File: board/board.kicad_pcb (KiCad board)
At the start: 2 copper layers, 41.1 x 15.7 mm, 14 parts, among them J1 Conn_01x05, P1 USB_C_Plug_USB2.0, U1 FT232RL

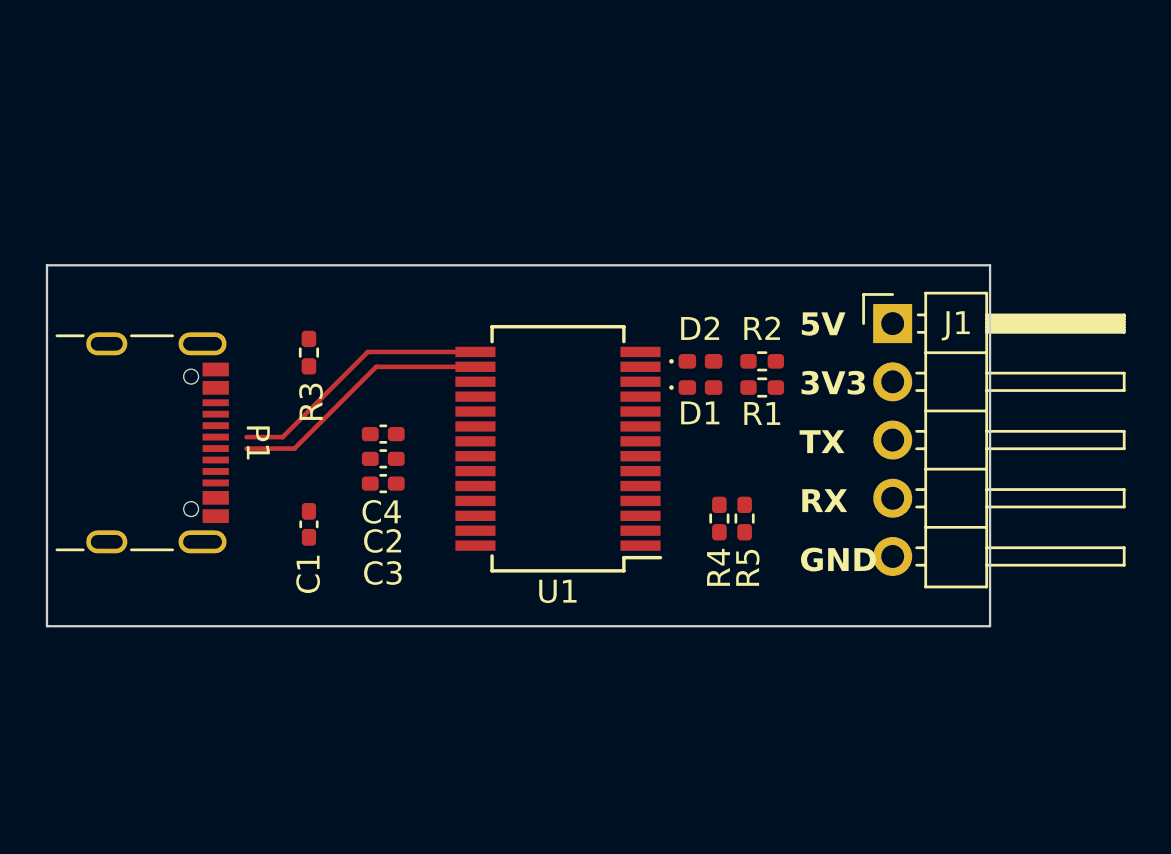
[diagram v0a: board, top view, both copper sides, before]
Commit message: feat(bsp/usb-ttl/debug): schematic
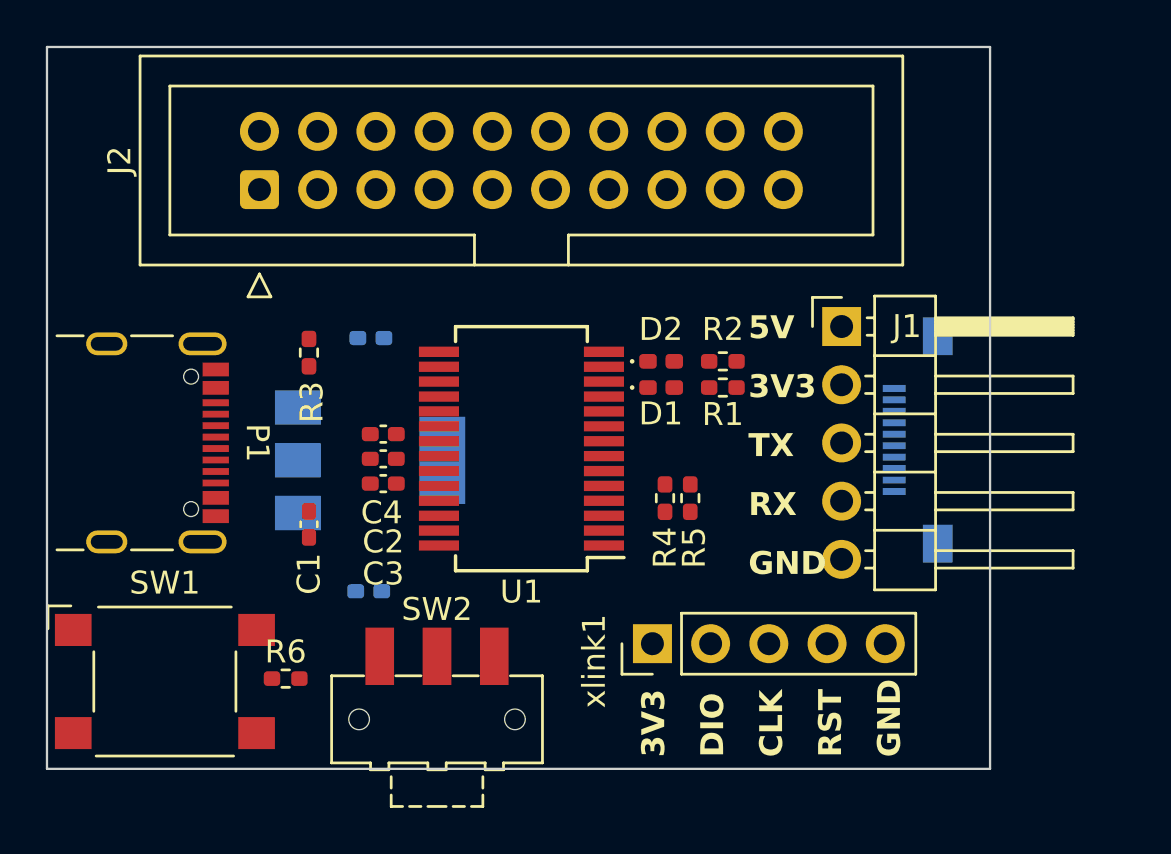
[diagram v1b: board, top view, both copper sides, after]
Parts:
- added C5: 10uF, Capacitor_SMD:C_0402_1005Metric_Pad0.74x0.62mm_HandSolder, B.Cu at (102.7, 90.6)
- added C6: 10uF, Capacitor_SMD:C_0402_1005Metric_Pad0.74x0.62mm_HandSolder, B.Cu at (102.6, 101.6)
- added J2: Conn_ARM_JTAG_SWD_20, Connector_IDC:IDC-Header_2x10_P2.54mm_Vertical, F.Cu at (97.8, 84.1)
- added J3: Conn_01x10, Connector_FFC-FPC:Molex_54548-1071_1x10-1MP_P0.5mm_Horizontal, B.Cu at (126.5, 95.0)
- added R6: 10K, Resistor_SMD:R_0402_1005Metric_Pad0.72x0.64mm_HandSolder, F.Cu at (98.9, 105.4)
- added SW1: RST, Button_Switch_SMD:SW_SPST_Omron_B3FS-100xP, F.Cu at (93.7, 105.5)
- added SW2: BOOT, Button_Switch_SMD:SW_SPDT_CK-JS102011SAQN, F.Cu at (105.5, 107.2)
- added U2: AMS1117-3.3, Package_TO_SOT_SMD:SOT-223-3_TabPin2, B.Cu at (102.6, 95.9)
- added xlink1: Conn_01x05, Connector_PinHeader_2.54mm:PinHeader_1x05_P2.54mm_Vertical, F.Cu at (114.9, 103.9)
- moved R4 2.53 mm to (115.5, 97.5)
- moved R5 2.53 mm to (116.6, 97.5)
- moved J1 2.23 mm to (123.2, 90.0)
- moved R1 1.72 mm to (118.0, 92.7)
- moved R2 1.72 mm to (118.0, 91.6)
- moved D1 1.72 mm to (115.3, 92.7)
- moved D2 1.72 mm to (115.3, 91.6)
- moved U1 1.59 mm to (109.2, 95.4)
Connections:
- C4 pad 1: +3.3V -> /3V3
- U1 pad 17: +3.3V -> /3V3
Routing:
- net /D+: track 11.5 -> 0.00 mm
- net /D-: track 11.5 -> 0.00 mm
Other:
- board size 41.1 x 15.7 mm -> 41.1 x 31.5 mm
- board text added: "CLK"
- board text added: "DIO"
- board text added: "RST"

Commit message: feat(bsp/usb-ttl/debug): pcb layer
aa
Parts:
- moved J3 45.7 mm to (169.1, 111.8)
- moved J1 45.5 mm to (164.7, 108.7)
- moved R4 43.9 mm to (154.9, 116.8)
- moved R6 43.7 mm to (138.7, 123.4), turned to -90 degrees
- moved SW2 43.0 mm to (144.7, 125.0)
- moved R1 42.8 mm to (156.5, 111.4)
- moved R2 42.8 mm to (156.5, 110.2)
- moved U2 42.8 mm to (141.1, 114.6)
- moved D1 42.8 mm to (153.8, 111.4)
- moved D2 42.8 mm to (153.8, 110.2)
- moved xlink1 42.8 mm to (153.4, 122.6)
- moved J2 42.8 mm to (136.3, 102.7)
- moved RST1 42.7 mm to (132.7, 122.9)
- moved C5 42.0 mm to (139.7, 110.2), turned to 0 degrees
- moved P1 41.9 mm to (130.7, 111.8)
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- renumbered SW1 to RST1
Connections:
- J3 pad 1: unconnected-(J3-Pin_1-Pad1) -> +3.3V
- J3 pad 2: unconnected-(J3-Pin_2-Pad2) -> /SWCLK
- J3 pad 3: +3.3V -> /SWDIO
- J3 pad 4: /BOOT -> unconnected-(J3-Pin_4-Pad4)
- J3 pad 5: /RST -> unconnected-(J3-Pin_5-Pad5)
- J3 pad 8: /SWCLK -> /RST
- J3 pad 9: /SWDIO -> /BOOT
- R6 pad 2: Net-(R6-Pad2) -> /RST
- RST1 pad 2: Net-(R6-Pad2) -> /RST
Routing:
- net +3.3V: track 0.00 -> 102.6 mm, vias 0 -> 1
- net /RST: track 0.00 -> 74.6 mm, vias 0 -> 3
- net /SWDIO: track 0.00 -> 68.2 mm, vias 0 -> 2
- net +5V: track 0.00 -> 58.0 mm, vias 0 -> 2
- net /SWCLK: track 0.00 -> 56.9 mm, vias 0 -> 2
- net /BOOT: track 0.00 -> 33.4 mm, vias 0 -> 1
- net /RX: track 0.00 -> 20.5 mm
- net /TX: track 0.00 -> 20.1 mm, vias 0 -> 2
- net GND: track 0.00 -> 14.2 mm, vias 0 -> 1
- net /RXLED: track 0.00 -> 11.8 mm, vias 0 -> 2
- net /D+: track 0.00 -> 11.4 mm
- net /D-: track 0.00 -> 11.3 mm
- net /TXLED: track 0.00 -> 9.91 mm, vias 0 -> 2
- net Net-(P1-CC): track 0.00 -> 5.53 mm
- net /3V3: track 0.00 -> 2.73 mm
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- added copper zone on B.Cu, net GND
- added copper zone on F.Cu, net GND
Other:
- board size 41.1 x 31.5 mm -> 45.7 x 30.5 mm
